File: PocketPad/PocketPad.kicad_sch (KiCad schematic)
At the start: 35 parts, among them SW0 SW_Push, SW1 SW_Push, SW10 SW_Push, SW11 SW_Push, SW12 SW_Push, SW13 SW_Push, SW14 SW_Push, SW15 SW_Push, SW16 SW_Push, SW2 SW_Push, SW3 SW_Push, SW4 SW_Push, SW5 SW_Push, SW6 SW_Push, SW7 SW_Push, SW8 SW_Push, SW9 SW_Push

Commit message: Replaced Diodes. Added 3D models
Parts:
- D0, D1, D10, D11, D12, D13, D14, D15, D16, D2, D3, D4, D5, D6, D7, D8, D9: footprint Diode_SMD:D_SOD-123 -> Diode_THT:D_DO-35_SOD27_P7.62mm_Horizontal
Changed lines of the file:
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@@
       (effects (font (size 1.27 1.27)) (justify left))
     )
-    (property "Footprint" "Diode_SMD:D_SOD-123" (id 2) (at 245.11 52.07 0)
+    (property "Footprint" "Diode_THT:D_DO-35_SOD27_P7.62mm_Horizontal" (id 2) (at 245.11 52.07 0)
       (effects (font (size 1.27 1.27)) hide)
     )
@@
       (effects (font (size 1.27 1.27)) (justify left))
     )
-    (property "Footprint" "Diode_SMD:D_SOD-123" (id 2) (at 233.68 31.75 0)
+    (property "Footprint" "Diode_THT:D_DO-35_SOD27_P7.62mm_Horizontal" (id 2) (at 233.68 31.75 0)
       (effects (font (size 1.27 1.27)) hide)
     )
@@
       (effects (font (size 1.27 1.27)) (justify left))
     )
-    (property "Footprint" "Diode_SMD:D_SOD-123" (id 2) (at 210.82 52.07 0)
+    (property "Footprint" "Diode_THT:D_DO-35_SOD27_P7.62mm_Horizontal" (id 2) (at 210.82 52.07 0)
       (effects (font (size 1.27 1.27)) hide)
     )
@@
       (effects (font (size 1.27 1.27)) (justify left))
     )
-    (property "Footprint" "Diode_SMD:D_SOD-123" (id 2) (at 217.17 31.75 0)
+    (property "Footprint" "Diode_THT:D_DO-35_SOD27_P7.62mm_Horizontal" (id 2) (at 217.17 31.75 0)
       (effects (font (size 1.27 1.27)) hide)
     )
@@
       (effects (font (size 1.27 1.27)) (justify left))
     )
-    (property "Footprint" "Diode_SMD:D_SOD-123" (id 2) (at 231.14 93.98 0)
+    (property "Footprint" "Diode_THT:D_DO-35_SOD27_P7.62mm_Horizontal" (id 2) (at 231.14 93.98 0)
       (effects (font (size 1.27 1.27)) hide)
     )
@@
       (effects (font (size 1.27 1.27)) (justify left))
     )
-    (property "Footprint" "Diode_SMD:D_SOD-123" (id 2) (at 247.65 93.98 0)
+    (property "Footprint" "Diode_THT:D_DO-35_SOD27_P7.62mm_Horizontal" (id 2) (at 247.65 93.98 0)
       (effects (font (size 1.27 1.27)) hide)
     )
@@
       (effects (font (size 1.27 1.27)) (justify left))
     )
-    (property "Footprint" "Diode_SMD:D_SOD-123" (id 2) (at 251.46 31.75 0)
+    (property "Footprint" "Diode_THT:D_DO-35_SOD27_P7.62mm_Horizontal" (id 2) (at 251.46 31.75 0)
       (effects (font (size 1.27 1.27)) hide)
     )
@@
       (effects (font (size 1.27 1.27)) (justify left))
     )
-    (property "Footprint" "Diode_SMD:D_SOD-123" (id 2) (at 267.97 31.75 0)
+    (property "Footprint" "Diode_THT:D_DO-35_SOD27_P7.62mm_Horizontal" (id 2) (at 267.97 31.75 0)
       (effects (font (size 1.27 1.27)) hide)
     )
@@
       (effects (font (size 1.27 1.27)) (justify left))
     )
-    (property "Footprint" "Diode_SMD:D_SOD-123" (id 2) (at 254 73.66 0)
+    (property "Footprint" "Diode_THT:D_DO-35_SOD27_P7.62mm_Horizontal" (id 2) (at 254 73.66 0)
       (effects (font (size 1.27 1.27)) hide)
     )
@@
       (effects (font (size 1.27 1.27)) (justify left))
     )
-    (property "Footprint" "Diode_SMD:D_SOD-123" (id 2) (at 190.5 118.11 0)
+    (property "Footprint" "Diode_THT:D_DO-35_SOD27_P7.62mm_Horizontal" (id 2) (at 190.5 118.11 0)
       (effects (font (size 1.27 1.27)) hide)
     )
@@
       (effects (font (size 1.27 1.27)) (justify left))
     )
-    (property "Footprint" "Diode_SMD:D_SOD-123" (id 2) (at 237.49 73.66 0)
+    (property "Footprint" "Diode_THT:D_DO-35_SOD27_P7.62mm_Horizontal" (id 2) (at 237.49 73.66 0)
       (effects (font (size 1.27 1.27)) hide)
     )
@@
       (effects (font (size 1.27 1.27)) (justify left))
     )
-    (property "Footprint" "Diode_SMD:D_SOD-123" (id 2) (at 196.85 93.98 0)
+    (property "Footprint" "Diode_THT:D_DO-35_SOD27_P7.62mm_Horizontal" (id 2) (at 196.85 93.98 0)
       (effects (font (size 1.27 1.27)) hide)
     )
@@
       (effects (font (size 1.27 1.27)) (justify left))
     )
-    (property "Footprint" "Diode_SMD:D_SOD-123" (id 2) (at 227.33 52.07 0)
+    (property "Footprint" "Diode_THT:D_DO-35_SOD27_P7.62mm_Horizontal" (id 2) (at 227.33 52.07 0)
       (effects (font (size 1.27 1.27)) hide)
     )
@@
       (effects (font (size 1.27 1.27)) (justify left))
     )
-    (property "Footprint" "Diode_SMD:D_SOD-123" (id 2) (at 261.62 52.07 0)
+    (property "Footprint" "Diode_THT:D_DO-35_SOD27_P7.62mm_Horizontal" (id 2) (at 261.62 52.07 0)
       (effects (font (size 1.27 1.27)) hide)
     )
@@
       (effects (font (size 1.27 1.27)) (justify left))
     )
-    (property "Footprint" "Diode_SMD:D_SOD-123" (id 2) (at 203.2 73.66 0)
+    (property "Footprint" "Diode_THT:D_DO-35_SOD27_P7.62mm_Horizontal" (id 2) (at 203.2 73.66 0)
       (effects (font (size 1.27 1.27)) hide)
     )
@@
       (effects (font (size 1.27 1.27)) (justify left))
     )
-    (property "Footprint" "Diode_SMD:D_SOD-123" (id 2) (at 213.36 93.98 0)
+    (property "Footprint" "Diode_THT:D_DO-35_SOD27_P7.62mm_Horizontal" (id 2) (at 213.36 93.98 0)
       (effects (font (size 1.27 1.27)) hide)
     )
@@
       (effects (font (size 1.27 1.27)) (justify left))
     )
-    (property "Footprint" "Diode_SMD:D_SOD-123" (id 2) (at 219.71 73.66 0)
+    (property "Footprint" "Diode_THT:D_DO-35_SOD27_P7.62mm_Horizontal" (id 2) (at 219.71 73.66 0)
       (effects (font (size 1.27 1.27)) hide)
     )
@@
   (symbol_instances
     (path "/632ca50b-899a-452a-bb30-e9691efaf0f0"
-      (reference "D0") (unit 1) (value "DIODE") (footprint "Diode_SMD:D_SOD-123")
+      (reference "D0") (unit 1) (value "DIODE") (footprint "Diode_THT:D_DO-35_SOD27_P7.62mm_Horizontal")
     )
     (path "/404a38f2-6947-4368-aeb6-92b71c21e752"
-      (reference "D1") (unit 1) (value "DIODE") (footprint "Diode_SMD:D_SOD-123")
+      (reference "D1") (unit 1) (value "DIODE") (footprint "Diode_THT:D_DO-35_SOD27_P7.62mm_Horizontal")
     )
     (path "/965737ea-63b4-49a3-b487-19550e23502c"
-      (reference "D2") (unit 1) (value "DIODE") (footprint "Diode_SMD:D_SOD-123")
+      (reference "D2") (unit 1) (value "DIODE") (footprint "Diode_THT:D_DO-35_SOD27_P7.62mm_Horizontal")
     )
     (path "/9daac2bc-5eca-4ecd-8aa1-c583dd1bd17b"
-      (reference "D3") (unit 1) (value "DIODE") (footprint "Diode_SMD:D_SOD-123")
+      (reference "D3") (unit 1) (value "DIODE") (footprint "Diode_THT:D_DO-35_SOD27_P7.62mm_Horizontal")
     )
     (path "/4de9e71d-0c97-44a2-b556-89e87c0667bc"
-      (reference "D4") (unit 1) (value "DIODE") (footprint "Diode_SMD:D_SOD-123")
+      (reference "D4") (unit 1) (value "DIODE") (footprint "Diode_THT:D_DO-35_SOD27_P7.62mm_Horizontal")
     )
     (path "/cd14994f-661e-4b09-b5e6-3499b926b985"
-      (reference "D5") (unit 1) (value "DIODE") (footprint "Diode_SMD:D_SOD-123")
+      (reference "D5") (unit 1) (value "DIODE") (footprint "Diode_THT:D_DO-35_SOD27_P7.62mm_Horizontal")
     )
     (path "/28b66d03-a827-4e0d-940a-f4ccc9f4a11a"
-      (reference "D6") (unit 1) (value "DIODE") (footprint "Diode_SMD:D_SOD-123")
+      (reference "D6") (unit 1) (value "DIODE") (footprint "Diode_THT:D_DO-35_SOD27_P7.62mm_Horizontal")
     )
     (path "/d2a08022-b002-4077-b1e4-369c330662b1"
-      (reference "D7") (unit 1) (value "DIODE") (footprint "Diode_SMD:D_SOD-123")
+      (reference "D7") (unit 1) (value "DIODE") (footprint "Diode_THT:D_DO-35_SOD27_P7.62mm_Horizontal")
     )
     (path "/e6a1239a-7517-4561-8d23-9db218d7f5cb"
-      (reference "D8") (unit 1) (value "DIODE") (footprint "Diode_SMD:D_SOD-123")
+      (reference "D8") (unit 1) (value "DIODE") (footprint "Diode_THT:D_DO-35_SOD27_P7.62mm_Horizontal")
     )
     (path "/f9382c76-eeb9-4a2b-b1ba-09b07da52288"
-      (reference "D9") (unit 1) (value "DIODE") (footprint "Diode_SMD:D_SOD-123")
+      (reference "D9") (unit 1) (value "DIODE") (footprint "Diode_THT:D_DO-35_SOD27_P7.62mm_Horizontal")
     )
     (path "/c4c3d39e-3854-471a-a715-80796768a165"
-      (reference "D10") (unit 1) (value "DIODE") (footprint "Diode_SMD:D_SOD-123")
+      (reference "D10") (unit 1) (value "DIODE") (footprint "Diode_THT:D_DO-35_SOD27_P7.62mm_Horizontal")
     )
     (path "/bd5541a0-428f-4024-b86d-5d1cff36dbf4"
-      (reference "D11") (unit 1) (value "DIODE") (footprint "Diode_SMD:D_SOD-123")
+      (reference "D11") (unit 1) (value "DIODE") (footprint "Diode_THT:D_DO-35_SOD27_P7.62mm_Horizontal")
     )
     (path "/cb495fc9-e1e3-4d16-800c-9e730462dced"
-      (reference "D12") (unit 1) (value "DIODE") (footprint "Diode_SMD:D_SOD-123")
+      (reference "D12") (unit 1) (value "DIODE") (footprint "Diode_THT:D_DO-35_SOD27_P7.62mm_Horizontal")
     )
     (path "/edeab9e1-b698-4f95-851e-b0008254d590"
-      (reference "D13") (unit 1) (value "DIODE") (footprint "Diode_SMD:D_SOD-123")
+      (reference "D13") (unit 1) (value "DIODE") (footprint "Diode_THT:D_DO-35_SOD27_P7.62mm_Horizontal")
     )
     (path "/84933e38-32bd-4780-8f2b-ac0197491603"
-      (reference "D14") (unit 1) (value "DIODE") (footprint "Diode_SMD:D_SOD-123")
+      (reference "D14") (unit 1) (value "DIODE") (footprint "Diode_THT:D_DO-35_SOD27_P7.62mm_Horizontal")
     )
     (path "/92e0f77f-45c2-4f92-9459-fdadaa841c8c"
-      (reference "D15") (unit 1) (value "DIODE") (footprint "Diode_SMD:D_SOD-123")
+      (reference "D15") (unit 1) (value "DIODE") (footprint "Diode_THT:D_DO-35_SOD27_P7.62mm_Horizontal")
     )
     (path "/c03d0973-2b2e-4c18-ad37-4bc39955e217"
-      (reference "D16") (unit 1) (value "DIODE") (footprint "Diode_SMD:D_SOD-123")
+      (reference "D16") (unit 1) (value "DIODE") (footprint "Diode_THT:D_DO-35_SOD27_P7.62mm_Horizontal")
     )
     (path "/997ac6b3-feea-4945-b5ae-fc1302bd8731"

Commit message: V0.1 Complete
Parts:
- added D17, D18: DIODE, Diode_THT:D_DO-35_SOD27_P7.62mm_Horizontal, symbol Simulation_SPICE:DIODE
- added SW17, SW18: SW_Push, Keebio:Switch_6x6x8.5, symbol Switch:SW_Push
- SW0, SW1, SW10, SW11, SW12, SW13, SW14, SW15, SW16, SW2, SW3, SW4, SW5, SW6, SW7, SW8, SW9: footprint Button_Switch_SMD:SW_SPST_PTS645 -> Keebio:Switch_6x6x8.5
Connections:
- net ROW0: now also MCU1.17 (A0/PF7)
- net ROW1: now also MCU1.18 (A1/PF6)
- net ROW2: now also MCU1.19 (A2/PF5)
- net ROW3: now also MCU1.20 (A3/PF4)
- net COL2: now reaches SW10.1, SW14.1, SW2.1, SW6.1
- net COL2: now also MCU1.27 (C7), SW18.1
- net COL0: now reaches SW0.1, SW12.1, SW16.1, SW4.1, SW8.1
- net COL0: now also MCU1.25 (B7)
- net COL1: now reaches SW1.1, SW13.1, SW5.1, SW9.1
- net COL1: now also MCU1.26 (D5), SW17.1
- net COL3: now reaches SW11.1, SW15.1, SW3.1, SW7.1
- net COL3: now also MCU1.28 (F1)
- net ROW4: now reaches MCU1.16 (15/PB1)
- net ROW4: now also D16.2 (K), D17.2 (K), D18.2 (K)
- new net: D18.1 (A), SW18.2
- new net: D17.1 (A), SW17.2
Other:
- moved on the sheet: D0, D1, D10, D11, D12, D13, D14, D15, D16, D2, D3, D4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

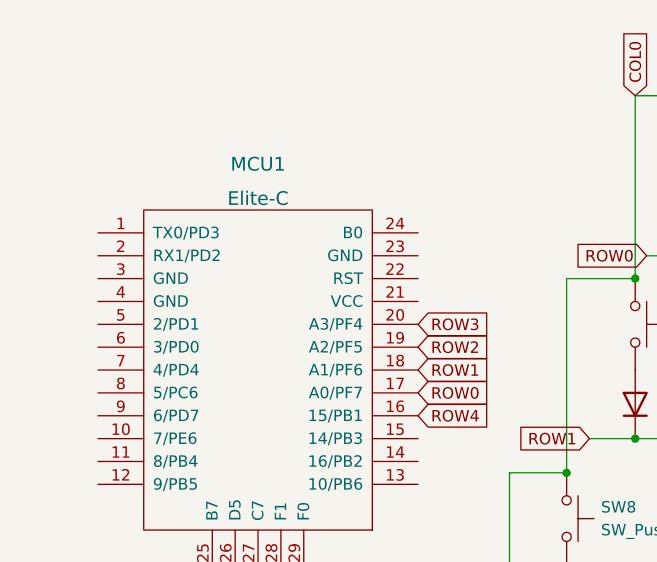
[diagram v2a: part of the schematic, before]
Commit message: Added GND plane
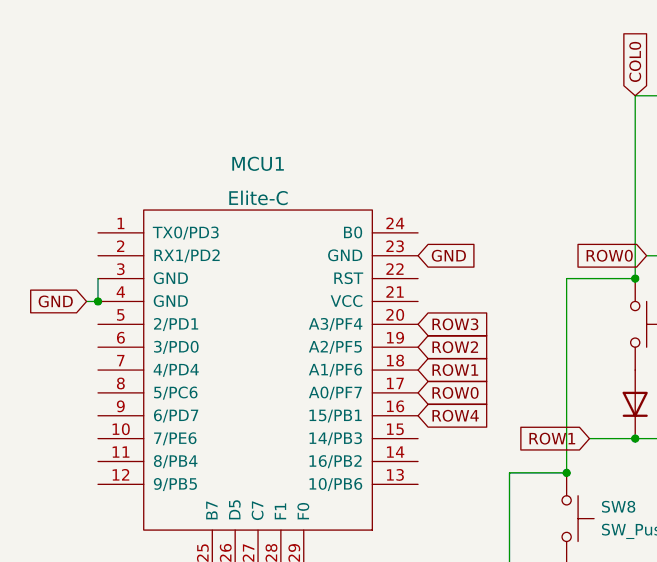
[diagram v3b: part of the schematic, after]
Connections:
- net GND: now reaches MCU1.23 (GND)
- net GND: now also MCU1.3 (GND), MCU1.4 (GND)
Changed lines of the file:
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@@
   (junction (at 100.33 43.18) (diameter 0) (color 0 0 0 0)
   )
+  (junction (at 34.29 48.26) (diameter 0) (color 0 0 0 0)
+  )
   (junction (at 73.66 129.54) (diameter 0) (color 0 0 0 0)
   )
@@
     (stroke (width 0) (type default) (color 0 0 0 0))
   )
+  (wire (pts (xy 34.29 45.72) (xy 34.29 48.26))
+    (stroke (width 0) (type default) (color 0 0 0 0))
+  )
   (wire (pts (xy 128.27 63.5) (xy 144.78 63.5))
     (stroke (width 0) (type default) (color 0 0 0 0))
@@
     (stroke (width 0) (type default) (color 0 0 0 0))
   )
+  (wire (pts (xy 33.02 48.26) (xy 34.29 48.26))
+    (stroke (width 0) (type default) (color 0 0 0 0))
+  )
   (wire (pts (xy 80.01 105.41) (xy 96.52 105.41))
     (stroke (width 0) (type default) (color 0 0 0 0))
@@
     )
   )
+  (global_label "GND" (shape input) (at 33.02 48.26 180) (fields_autoplaced)
+    (effects (font (size 1.27 1.27)) (justify right))
+    (property "Intersheet References" "${INTERSHEET_REFS}" (id 0) (at 26.7364 48.1806 0)
+      (effects (font (size 1.27 1.27)) (justify right) hide)
+    )
+  )
   (global_label "COL0" (shape input) (at 93.98 25.4 90) (fields_autoplaced)
     (effects (font (size 1.27 1.27)) (justify left))
@@
       (effects (font (size 1.27 1.27)) (justify left) hide)
     )
+  )
+  (global_label "GND" (shape input) (at 69.85 43.18 0) (fields_autoplaced)
+    (effects (font (size 1.27 1.27)) (justify left))
+    (property "Intersheet References" "${INTERSHEET_REFS}" (id 0) (at 76.1336 43.2594 0)
+      (effects (font (size 1.27 1.27)) (justify left) hide)
+    )

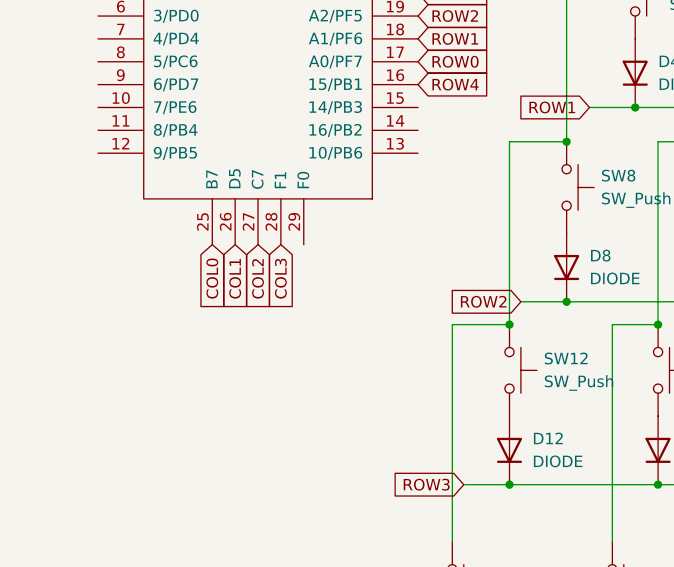
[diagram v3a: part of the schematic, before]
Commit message: Replaced Footprints and THT 3D Model
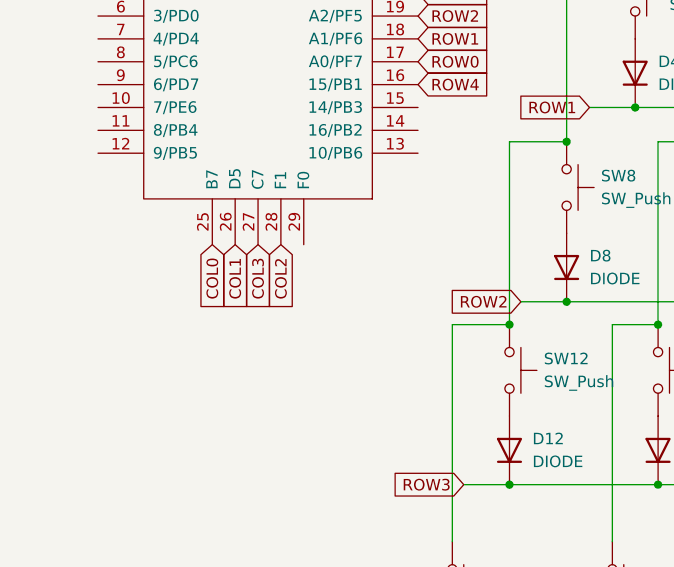
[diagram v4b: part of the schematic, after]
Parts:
- SW0, SW1, SW10, SW11, SW12, SW13, SW14, SW15, SW16, SW17, SW18, SW2, SW3, SW4, SW5, SW6, SW7, SW8, SW9: footprint Keebio:Switch_6x6x8.5 -> Keebio:Switch_THT_6x6x8.5
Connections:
- net COL2: now also MCU1.28 (F1); no longer MCU1.27 (C7)
- net COL3: now also MCU1.27 (C7); no longer MCU1.28 (F1)

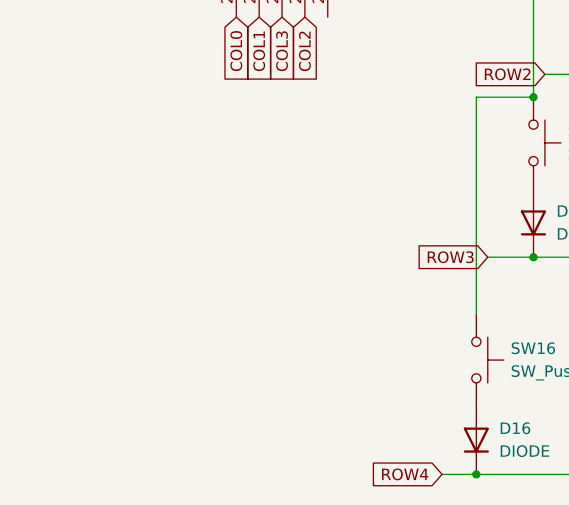
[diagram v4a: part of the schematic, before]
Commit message: Readded models and replaced footprint. Silkscreen done
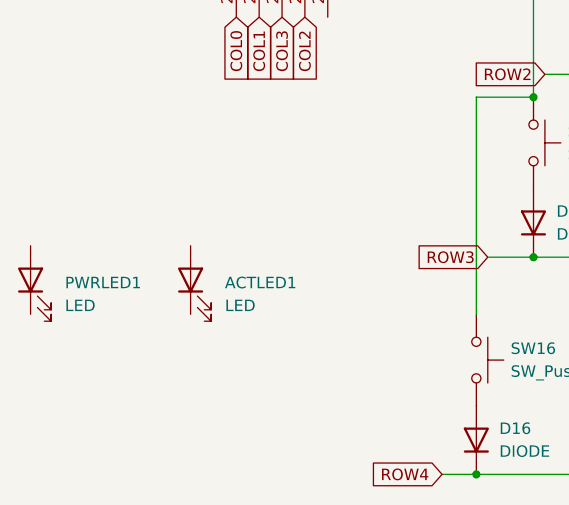
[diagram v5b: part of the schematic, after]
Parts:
- added ACTLED1, PWRLED1: LED, Keebio:LED_3mm, symbol Device:LED
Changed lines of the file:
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@@
+    (pin "2")
+  )
+  (symbol (lib_id "Device:LED") (at 41.91 107.95 90) (unit 1)
+    (in_bom yes) (on_board yes) (fields_autoplaced)
+    (property "Reference" "ACTLED1" (id 0) (at 45.72 108.2674 90)
+      (effects (font (size 1.27 1.27)) (justify right))
+    )
+    (property "Value" "LED" (id 1) (at 45.72 110.8074 90)
+      (effects (font (size 1.27 1.27)) (justify right))
+    )
+    (property "Footprint" "Keebio:LED_3mm" (id 2) (at 41.91 107.95 0)
+      (effects (font (size 1.27 1.27)) hide)
+    )
+    (property "Datasheet" "~" (id 3) (at 41.91 107.95 0)
+      (effects (font (size 1.27 1.27)) hide)
+    )
+    (pin "1")
     (pin "2")
   )
@@
     (pin "2")
   )
+  (symbol (lib_id "Device:LED") (at 24.13 107.95 90) (unit 1)
+    (in_bom yes) (on_board yes) (fields_autoplaced)
+    (property "Reference" "PWRLED1" (id 0) (at 27.94 108.2674 90)
+      (effects (font (size 1.27 1.27)) (justify right))
+    )
+    (property "Value" "LED" (id 1) (at 27.94 110.8074 90)
+      (effects (font (size 1.27 1.27)) (justify right))
+    )
+    (property "Footprint" "Keebio:LED_3mm" (id 2) (at 24.13 107.95 0)
+      (effects (font (size 1.27 1.27)) hide)
+    )
+    (property "Datasheet" "~" (id 3) (at 24.13 107.95 0)
+      (effects (font (size 1.27 1.27)) hide)
+    )
+    (pin "1")
+    (pin "2")
+  )
   (symbol (lib_id "Simulation_SPICE:DIODE") (at 80.01 101.6 270) (unit 1)
     (in_bom yes) (on_board yes) (fields_autoplaced)
@@
   )
   (symbol_instances
+    (path "/5aca0ffd-8f46-4634-bcbc-76cff0835fef"
+      (reference "ACTLED1") (unit 1) (value "LED") (footprint "Keebio:LED_3mm")
+    )
     (path "/632ca50b-899a-452a-bb30-e9691efaf0f0"
       (reference "D0") (unit 1) (value "DIODE") (footprint "Diode_THT:D_DO-35_SOD27_P7.62mm_Horizontal")
@@
       (reference "MCU1") (unit 1) (value "Elite-C") (footprint "Keebio:Elite-C")
     )
+    (path "/c8483ffe-b5bb-442a-b971-4fa85f1d23e8"
+      (reference "PWRLED1") (unit 1) (value "LED") (footprint "Keebio:LED_3mm")
+    )
     (path "/86a0a74c-a216-40d1-82dd-f646e6b8d5d3"
